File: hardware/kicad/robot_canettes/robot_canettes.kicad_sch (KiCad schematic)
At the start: 0 parts

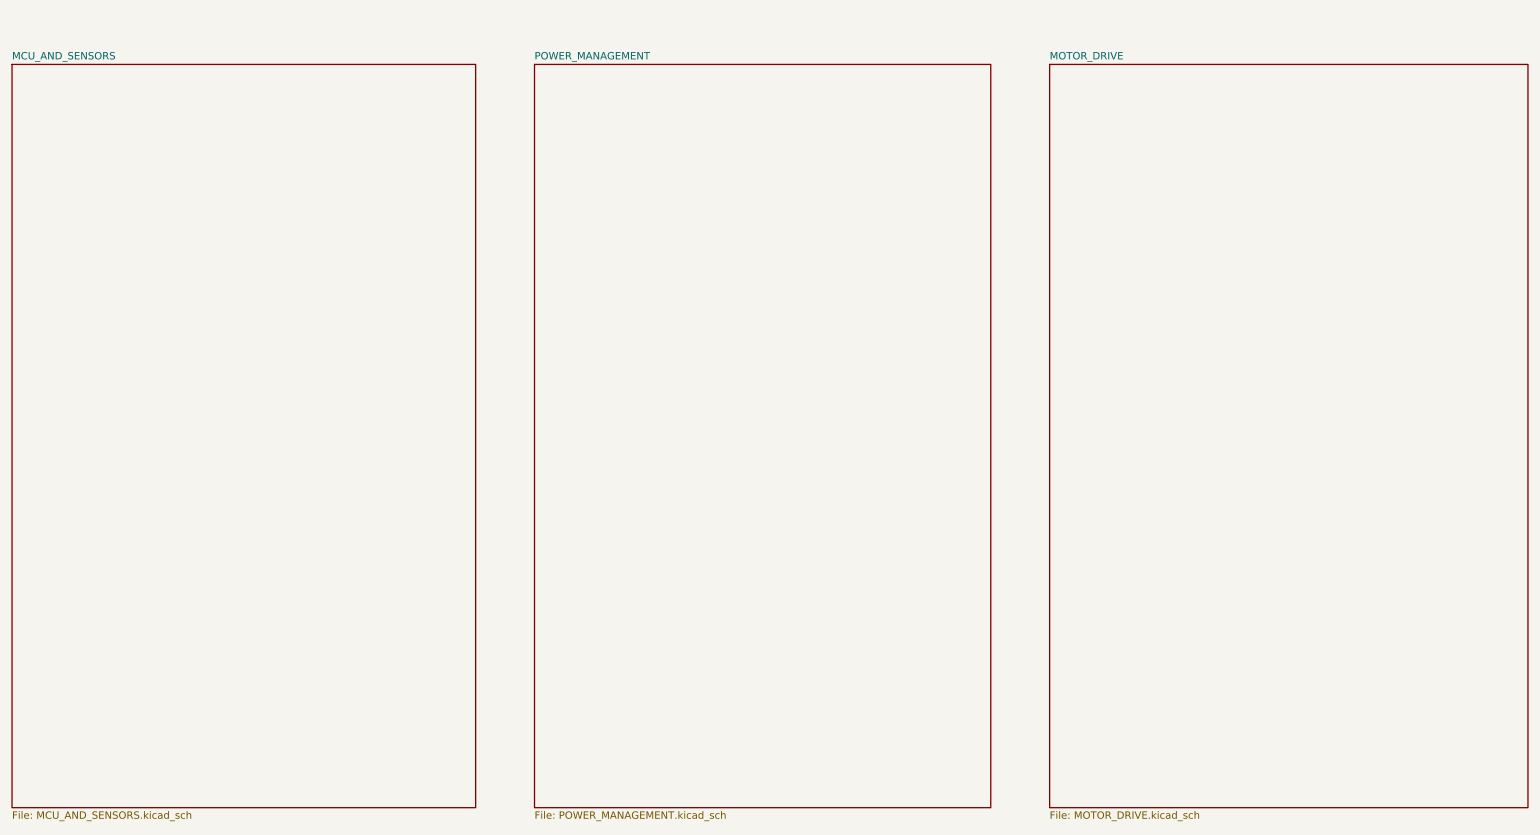
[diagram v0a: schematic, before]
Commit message: Ajout schema MCU et capteurs (02_MCU_AND_SENSORS)
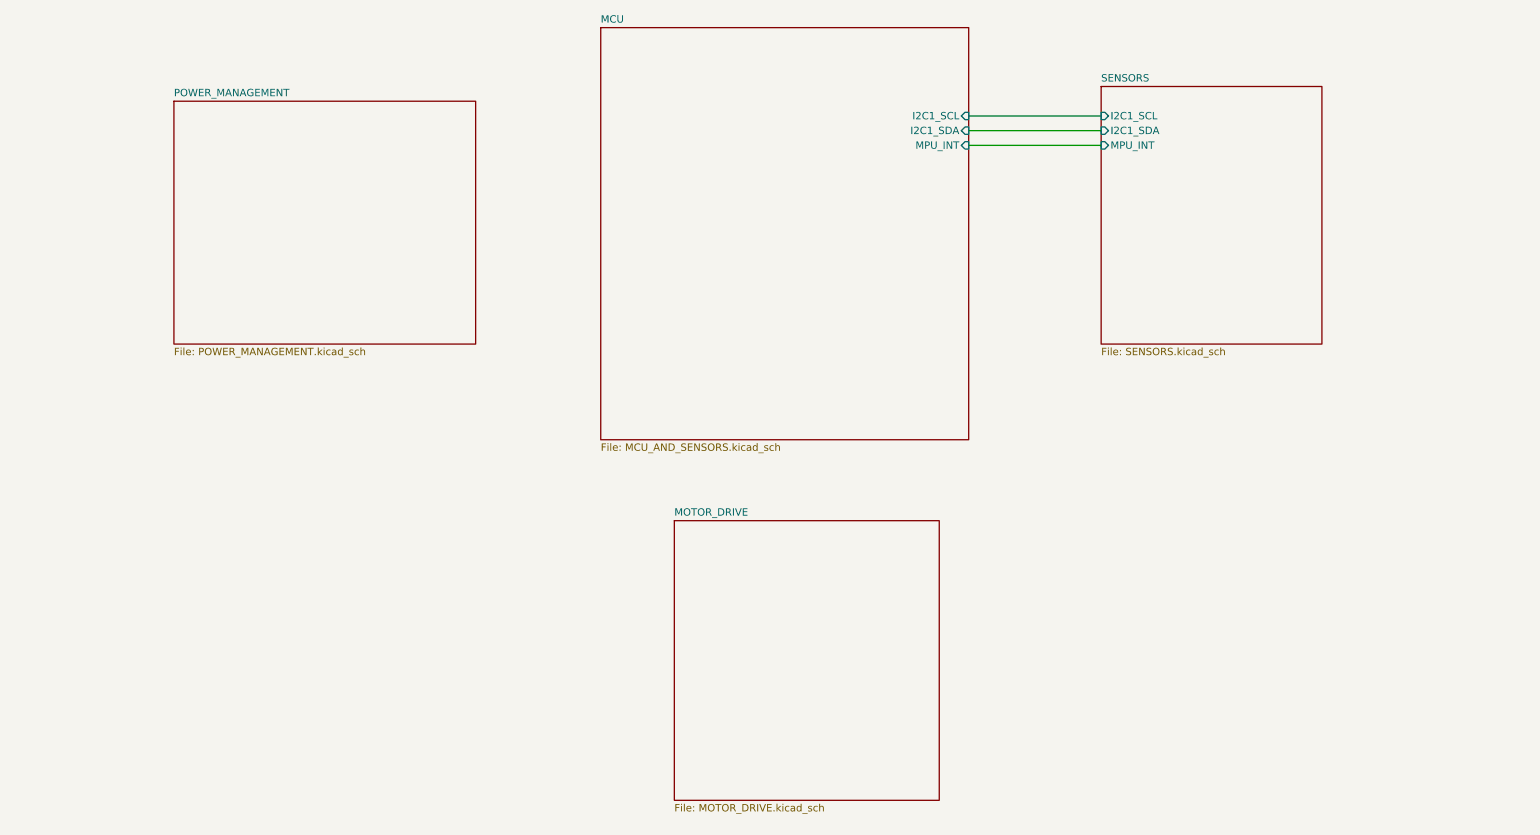
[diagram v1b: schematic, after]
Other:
- sheet MCU_AND_SENSORS renamed MCU
- added sheet SENSORS (SENSORS.kicad_sch)
- sheet MCU ports: added I2C1_SCL, I2C1_SDA, MPU_INT; removed none
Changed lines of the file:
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@@
 	(generator_version "10.0")
 	(paper "A4")
-	(sheet
-		(at 107.95 35.56)
-		(size 78.74 128.27)
+	(wire
+		(pts
+			(xy 182.88 49.53) (xy 205.74 49.53)
+		)
+		(stroke
+			(width 0)
+			(type default)
+		)
+	)
+	(wire
+		(pts
+			(xy 182.88 44.45) (xy 205.74 44.45)
+		)
+		(stroke
+			(width 0)
+			(type default)
+		)
+	)
+	(wire
+		(pts
+			(xy 182.88 46.99) (xy 205.74 46.99)
+		)
+		(stroke
+			(width 0)
+			(type default)
+		)
+	)
+	(sheet
+		(at 45.72 41.91)
+		(size 52.07 41.91)
 		(exclude_from_sim no)
 		(in_bom yes)
@@
 		)
 		(property "Sheetname" "POWER_MANAGEMENT"
-			(at 107.95 34.8484 0)
+			(at 45.72 41.1984 0)
 			(show_name no)
 			(do_not_autoplace no)
@@
 		)
 		(property "Sheetfile" "POWER_MANAGEMENT.kicad_sch"
-			(at 107.95 164.4146 0)
+			(at 45.72 84.4046 0)
 			(show_name no)
 			(do_not_autoplace no)
@@
 	)
 	(sheet
-		(at 17.78 35.56)
-		(size 80.01 128.27)
-		(exclude_from_sim no)
-		(in_bom yes)
-		(on_board yes)
-		(dnp no)
-		(fields_autoplaced yes)
-		(stroke
-			(width 0.1524)
-			(type solid)
-		)
-		(fill
-			(color 0 0 0 0)
-		)
-		(property "Sheetname" "MCU_AND_SENSORS"
-			(at 17.78 34.8484 0)
+		(at 205.74 39.37)
+		(size 38.1 44.45)
+		(exclude_from_sim no)
+		(in_bom yes)
+		(on_board yes)
+		(dnp no)
+		(fields_autoplaced yes)
+		(stroke
+			(width 0.1524)
+			(type solid)
+		)
+		(fill
+			(color 0 0 0 0)
+		)
+		(property "Sheetname" "SENSORS"
+			(at 205.74 38.6584 0)
+			(show_name no)
+			(do_not_autoplace no)
+			(effects
+				(font
+					(size 1.27 1.27)
+				)
+				(justify left bottom)
+			)
+		)
+		(property "Sheetfile" "SENSORS.kicad_sch"
+			(at 205.74 84.4046 0)
+			(show_name no)
+			(do_not_autoplace no)
+			(effects
+				(font
+					(size 1.27 1.27)
+				)
+				(justify left top)
+			)
+		)
+		(pin "I2C1_SCL" input
+			(at 205.74 44.45 180)
+			(effects
+				(font
+					(size 1.27 1.27)
+				)
+				(justify left)
+			)
+		)
+		(pin "I2C1_SDA" input
+			(at 205.74 46.99 180)
+			(effects
+				(font
+					(size 1.27 1.27)
+				)
+				(justify left)
+			)
+		)
+		(pin "MPU_INT" input
+			(at 205.74 49.53 180)
+			(effects
+				(font
+					(size 1.27 1.27)
+				)
+				(justify left)
+			)
+		)
+		(instances
+			(project "robot_canettes"
+				(path "/67ea9330-6bd8-4bfd-bb5f-e77247705b59"
+					(page "5")
+				)
+			)
+		)
+	)
+	(sheet
+		(at 119.38 29.21)
+		(size 63.5 71.12)
+		(exclude_from_sim no)
+		(in_bom yes)
+		(on_board yes)
+		(dnp no)
+		(fields_autoplaced yes)
+		(stroke
+			(width 0.1524)
+			(type solid)
+		)
+		(fill
+			(color 0 0 0 0)
+		)
+		(property "Sheetname" "MCU"
+			(at 119.38 28.4984 0)
 			(show_name no)
 			(do_not_autoplace no)
@@
 		)
 		(property "Sheetfile" "MCU_AND_SENSORS.kicad_sch"
-			(at 17.78 164.4146 0)
+			(at 119.38 100.9146 0)
 			(show_name no)
 			(do_not_autoplace no)
@@
 				)
 				(justify left top)
+			)
+		)
+		(pin "I2C1_SCL" input
+			(at 182.88 44.45 0)
+			(effects
+				(font
+					(size 1.27 1.27)
+				)
+				(justify right)
+			)
+		)
+		(pin "I2C1_SDA" input
+			(at 182.88 46.99 0)
+			(effects
+				(font
+					(size 1.27 1.27)
+				)
+				(justify right)
+			)
+		)
+		(pin "MPU_INT" input
+			(at 182.88 49.53 0)
+			(effects
+				(font
+					(size 1.27 1.27)
+				)
+				(justify right)
 			)
 		)
@@
 	)
 	(sheet
-		(at 196.85 35.56)
-		(size 82.55 128.27)
+		(at 132.08 114.3)
+		(size 45.72 48.26)
 		(exclude_from_sim no)
 		(in_bom yes)
@@
 		)
 		(property "Sheetname" "MOTOR_DRIVE"
-			(at 196.85 34.8484 0)
+			(at 132.08 113.5884 0)
 			(show_name no)
 			(do_not_autoplace no)
@@
 		)
 		(property "Sheetfile" "MOTOR_DRIVE.kicad_sch"
-			(at 196.85 164.4146 0)
-			(show_name no)
-			(do_not_autoplace no)
+			(at 132.08 163.1446 0)
+			(show_name no)
+			(do_not_autoplace no)
